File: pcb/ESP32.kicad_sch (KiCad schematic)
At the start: 7 parts, among them U4 ESP32-WROOM-32E

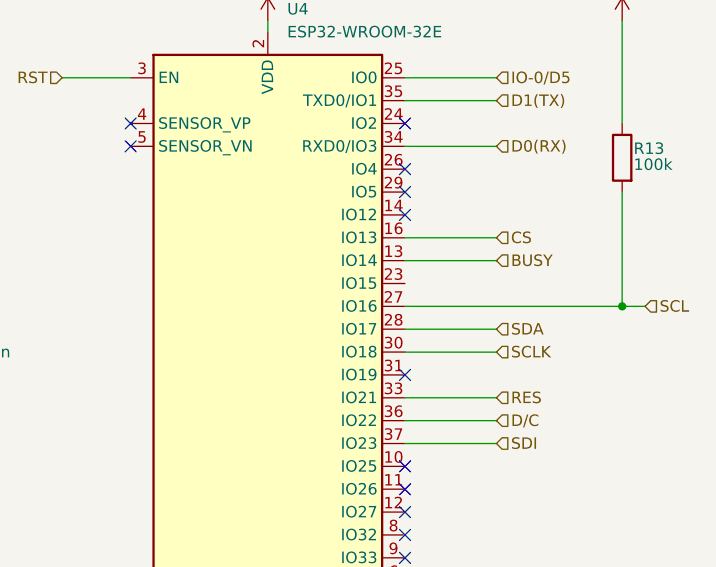
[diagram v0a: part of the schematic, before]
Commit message: switch epaper capacitor to 0402
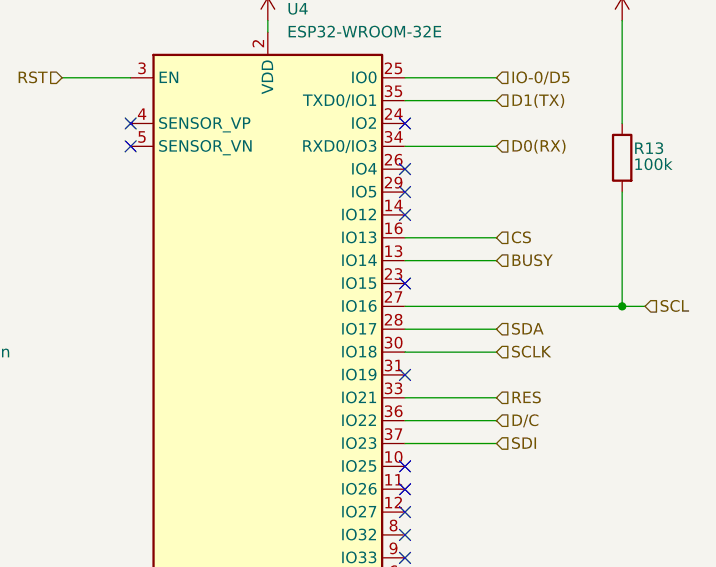
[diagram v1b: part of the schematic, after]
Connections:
- no-connect marks 13 -> 14
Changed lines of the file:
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@@
+	)
+	(no_connect
+		(at 179.07 88.9)
 	)
 	(no_connect
